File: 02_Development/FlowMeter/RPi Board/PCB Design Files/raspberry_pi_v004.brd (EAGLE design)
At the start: 111.8 x 128.3 mm, 116 parts, among them J5 POWER_JACK, P1 SPL006-007, P2 SPL006-007, P3 SPL006-007, P4 SPL006-007, P5 SPL006-007, Q1 4.3A/20V/54mΩ, Q2 500mA/300V, U6 TCA9548APWR, U7 TCA9548APWR

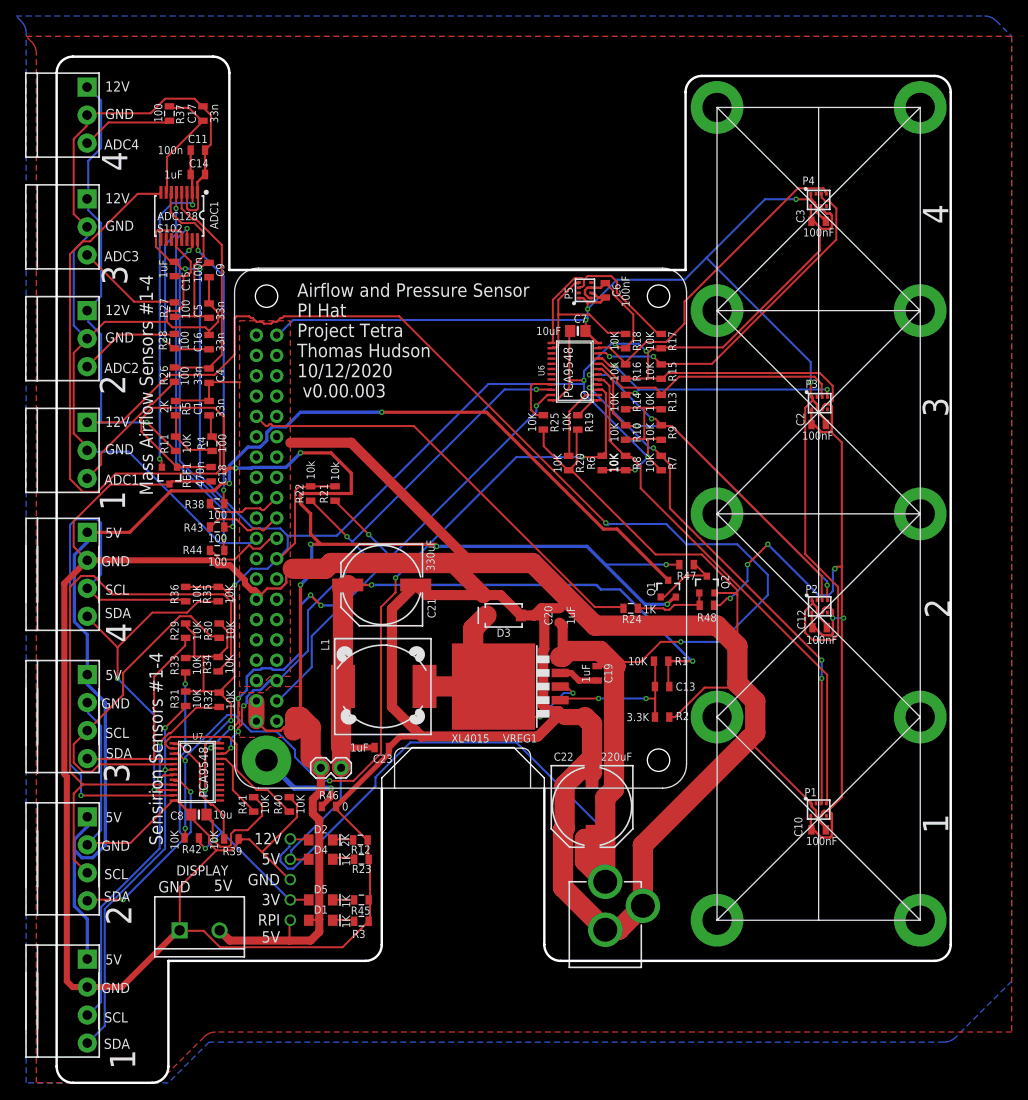
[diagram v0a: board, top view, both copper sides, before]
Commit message: added new 5V regulator
added new 5V regulator as existing regulator was out-of-stock at JLCPCB
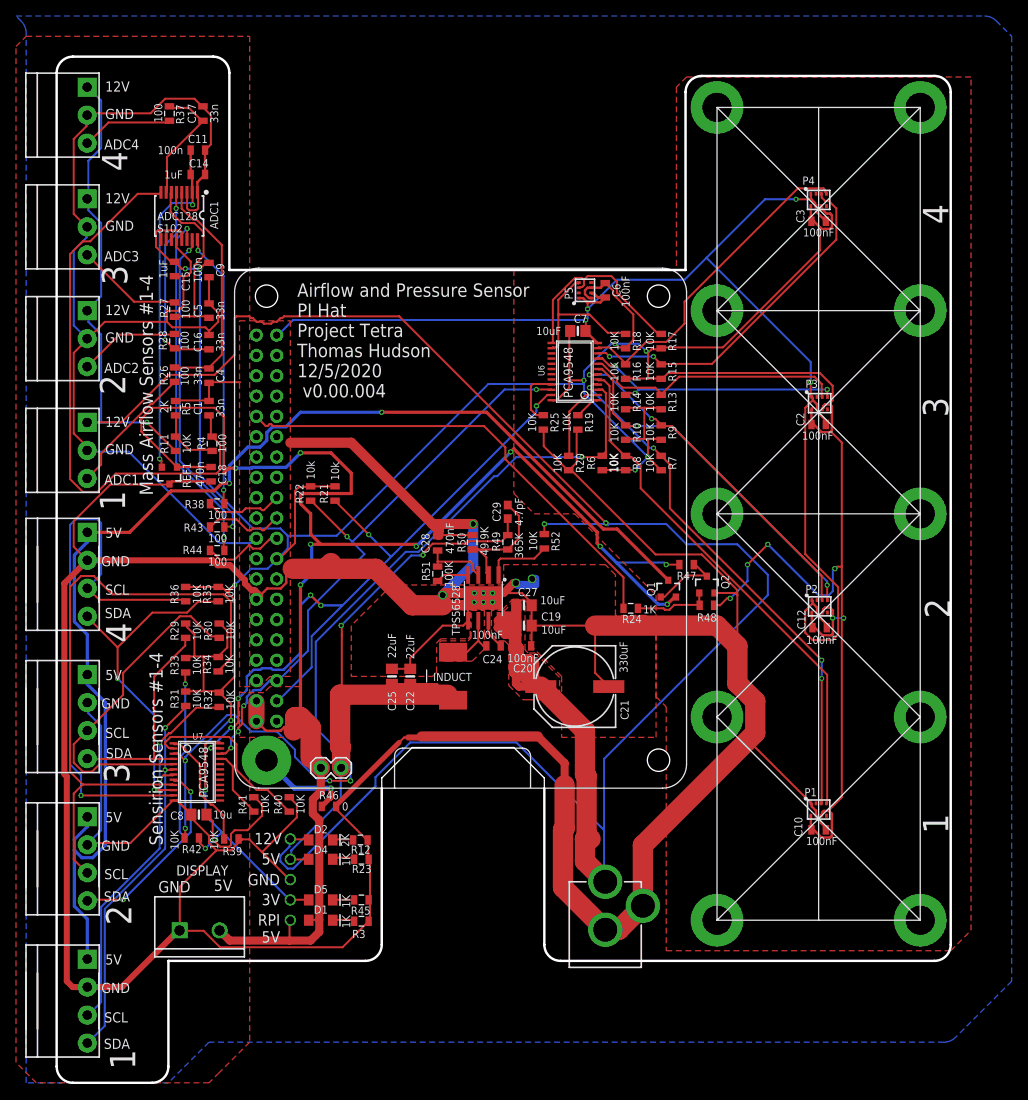
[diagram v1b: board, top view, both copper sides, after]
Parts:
- removed C13: 33n, SparkFun-Capacitors:0805
- removed C23: 1uF, SparkFun-Capacitors:0805
- removed D3: 3A/40V/500mV, SparkFun-DiscreteSemi:SMA-DIODE
- removed L1: INDUCTOR12.5, th_libraries:INDUCTOR_12.5X12.5
- removed R1: 10K, SparkFun-Resistors:0805
- removed R2: 3.3K, SparkFun-Resistors:0805
- removed VREG1: XL4015, th_libraries:TO263-5
- added C24: 100nF, SparkFun-Capacitors:0805
- added C25: 22uF, microbuilder:0805-NO
- added C27: 10uF, microbuilder:0805-NO
- added C28: 470nF, SparkFun-Capacitors:0805
- added C29: 4.7pF, SparkFun-Capacitors:0603
- added INDUCT: INDUCTOR_6.6_7.3, th_libraries:INDUCTOR_6.6_7.3
- added R49: 365K, SparkFun-Passives:0805
- added R50: 49.9K, SparkFun-Passives:0805
- added R51: 100K, SparkFun-Passives:0805
- added R52: 10K, SparkFun-Resistors:0805
- added TPS: TPS56528, th_libraries:SOIC8_POWER
- C19: value 1uF -> 10uF; device SparkFun-Capacitors:0805 -> microbuilder:0805-NO
- C20: value 1uF -> 100nF
- C22: value 220uF -> 22uF; device SparkFun-Capacitors:PANASONIC_G -> microbuilder:0805-NO
- moved C22 27.9 mm to (13.7, -20.3), turned to 90 degrees
- moved C21 27.3 mm to (34.3, -21.6)
- moved C19 10.9 mm to (27.9, -14.0), turned to 0 degrees
- moved C20 5.85 mm to (27.9, -16.5), turned to 0 degrees
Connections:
- new net N$14: C24.1, TPS.7
- new net N$17: R51.1, TPS.4
- new net N$27: R52.2, TPS.1
- net 12V: now also C21.+, C27.1, R52.1, TPS.8; no longer C22.+, VREG1.5
- net 5V: now also C22.1, C25.1, C29.1, INDUCT.2, R49.2; no longer C13.1, C21.+, C23.1, L1.1, R1.1
- net GND: now also C19.2, C22.2, C25.2, C27.2, C28.2, R50.2, TPS.5, TPS.9; no longer C22.-, C23.2, D3.A, R2.2, VREG1.1
- net N$11: now also C29.2, R49.1, R50.1, TPS.2; no longer C13.2, R1.2, R2.1, VREG1.2
- net N$6: now also C24.2, INDUCT.1, TPS.6; no longer D3.C, L1.2, VREG1.3, VREG1.6
- net N$7: now also C28.1, R51.2, TPS.3; no longer C19.2, VREG1.4
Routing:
- net 12V: track 304.9 -> 355.7 mm
- net N$6: track 34.7 -> 7.53 mm, vias 2 -> 0
- net GND: track 900.3 -> 882.2 mm, vias 4 -> 14
- net 5V: track 97.9 -> 85.1 mm
- net PI_5V_POWER: track 202.1 -> 211.8 mm, vias 7 -> 9
- net N$27: track 0.00 -> 8.15 mm
- net N$11: track 21.5 -> 14.9 mm, vias 2 -> 0
- net RESET: track 108.2 -> 112.8 mm
- net N$17: track 0.00 -> 4.12 mm
- net N$14: track 0.00 -> 3.79 mm
- net GPIO12: track 56.0 -> 59.4 mm
- net N$7: track 5.02 -> 8.17 mm
- added copper zone on layer 1, net 12V
- added copper zone on layer 1, net N$6
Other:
- board text added: "Airflow and Pressure Sensor PI Hat Project Tetra Thomas Hudson 12/5/2020 v0.00.004"
- board text removed: "Airflow and Pressure Sensor PI Hat Project Tetra Thomas Hudson 10/12/2020 v0.00.003"

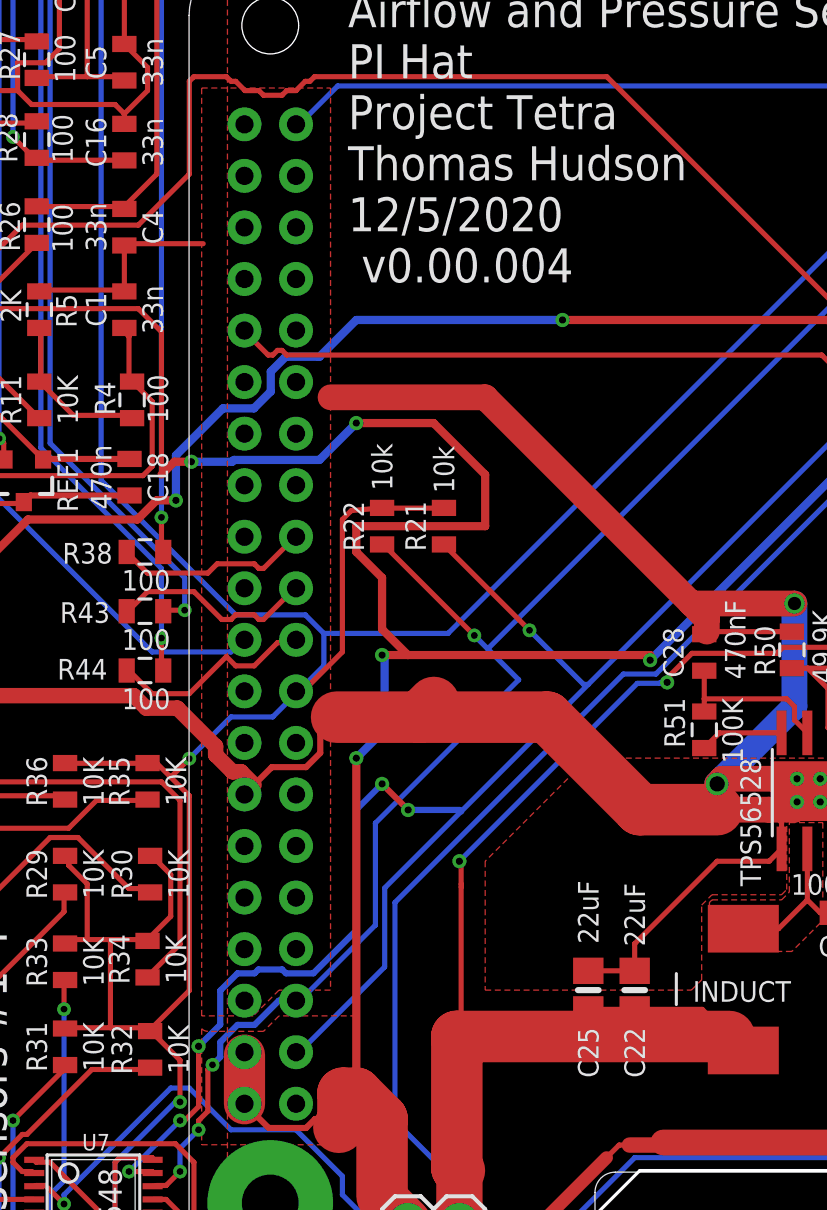
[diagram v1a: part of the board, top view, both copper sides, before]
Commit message: updated capacitor
changed C22 and C25 to 1206 footprint and specified 2mohm low ESR cap
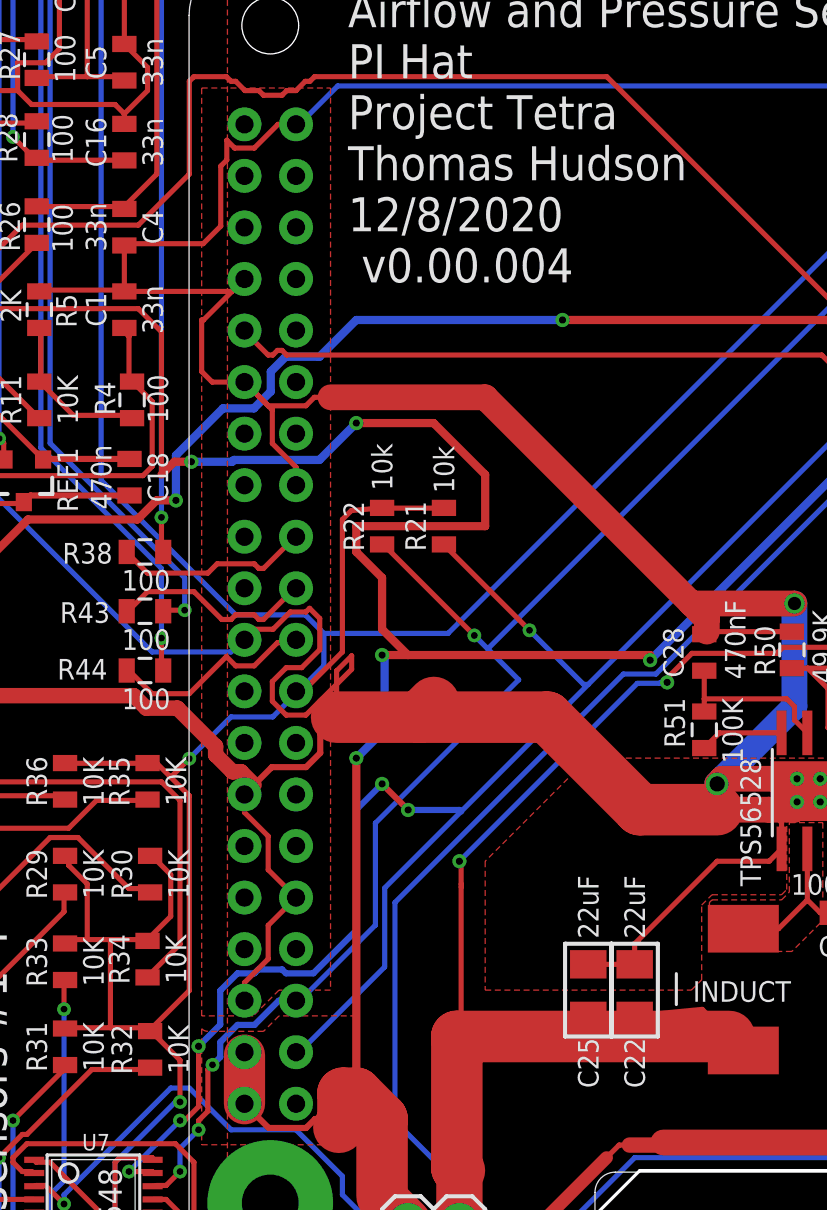
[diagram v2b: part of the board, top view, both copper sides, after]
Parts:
- C22, C25: device microbuilder:0805-NO -> microbuilder:_1206
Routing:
- net GND: track 882.2 -> 948.0 mm
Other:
- board text added: "Airflow and Pressure Sensor PI Hat Project Tetra Thomas Hudson 12/8/2020 v0.00.004"
- board text removed: "Airflow and Pressure Sensor PI Hat Project Tetra Thomas Hudson 12/5/2020 v0.00.004"
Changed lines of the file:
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@@
 Project Tetra
 Thomas Hudson
-12/5/2020
+12/8/2020
  v0.00.004</text>
 <text x="-17.2212" y="-17.2974" size="1.6764" layer="21" ratio="15" rot="R90" align="bottom-right">Sensirion Sensors #1-4</text>
@@
 <attribute name="NAME" x="19" y="-20.895" size="1.016" layer="21" font="vector" ratio="15" align="bottom-center"/>
 </element>
-<element name="C22" library="microbuilder" package="0805-NO" value="22uF" x="13.716" y="-20.32" smashed="yes" rot="R90">
-<attribute name="NAME" x="14.224" y="-24.638" size="1.016" layer="21" ratio="15" rot="R90"/>
-<attribute name="VALUE" x="14.224" y="-18.161" size="1.016" layer="21" ratio="15" rot="R90"/>
-</element>
-<element name="C25" library="microbuilder" package="0805-NO" value="22uF" x="11.43" y="-20.32" smashed="yes" rot="R90">
-<attribute name="NAME" x="11.938" y="-24.638" size="1.016" layer="21" ratio="15" rot="R90"/>
-<attribute name="VALUE" x="11.938" y="-18.034" size="1.016" layer="21" ratio="15" rot="R90"/>
+<element name="C22" library="microbuilder" package="_1206" value="22uF" x="13.716" y="-20.32" smashed="yes" rot="R90">
+<attribute name="NAME" x="14.224" y="-25.146" size="1.016" layer="21" ratio="15" rot="R90"/>
+<attribute name="VALUE" x="14.224" y="-17.78" size="1.016" layer="21" ratio="15" rot="R90"/>
+</element>
+<element name="C25" library="microbuilder" package="_1206" value="22uF" x="11.43" y="-20.32" smashed="yes" rot="R90">
+<attribute name="NAME" x="11.938" y="-25.146" size="1.016" layer="21" ratio="15" rot="R90"/>
+<attribute name="VALUE" x="11.938" y="-17.78" size="1.016" layer="21" ratio="15" rot="R90"/>
 </element>
 </elements>
@@
 <wire x1="35.8902" y1="25.6032" x2="39.5478" y2="29.2608" width="0.254" layer="16"/>
 <wire x1="63.7794" y1="39.3192" x2="63.823546875" y2="39.363346875" width="0.254" layer="1"/>
-<wire x1="-7.5438" y1="16.4592" x2="-11.43" y2="16.4592" width="0.254" layer="1"/>
+<wire x1="-11.43" y1="16.4592" x2="-7.5438" y2="16.4592" width="0.254" layer="1"/>
 <wire x1="-11.43" y1="16.4592" x2="-11.43" y2="16.372" width="0.254" layer="1"/>
 <wire x1="33.6042" y1="5.2578" x2="34.0614" y2="5.2578" width="0.254" layer="1"/>
@@
 <wire x1="-26.647" y1="-59.152" x2="-22.3474" y2="-59.152" width="0.762" layer="1"/>
 <wire x1="-22.3474" y1="-59.152" x2="-15.3162" y2="-52.1208" width="0.762" layer="1"/>
-<wire x1="-1.27" y1="8.89" x2="6.35" y2="8.89" width="1.27" layer="1"/>
+<wire x1="6.35" y1="8.89" x2="-1.27" y2="8.89" width="1.27" layer="1"/>
 <polygon width="2.032" layer="16" isolate="0.000253125">
 <vertex x="-35.56" y="62.23"/>
@@
 <wire x1="33.02" y1="-33.909" x2="33.02" y2="-31.16600625" width="1.016" layer="1"/>
 <wire x1="33.02" y1="-31.16600625" x2="29.68219375" y2="-27.8282" width="1.016" layer="1"/>
-<wire x1="11.43" y1="-19.37" x2="13.716" y2="-19.37" width="0.254" layer="1"/>
+<wire x1="11.43" y1="-19.05" x2="13.716" y2="-19.05" width="0.254" layer="1"/>
 <wire x1="20.955" y1="-13.3604" x2="20.3454" y2="-13.97" width="0.254" layer="1"/>
 <wire x1="20.3454" y1="-13.97" x2="17.78" y2="-13.97" width="0.254" layer="1"/>
 <wire x1="17.78" y1="-13.97" x2="13.716" y2="-18.034" width="0.254" layer="1"/>
-<wire x1="13.716" y1="-18.034" x2="13.716" y2="-19.37" width="0.254" layer="1"/>
+<wire x1="13.716" y1="-18.034" x2="13.716" y2="-19.05" width="0.254" layer="1"/>
 <wire x1="28.89" y1="-11.43" x2="28.89" y2="-13.97" width="0.254" layer="1"/>
 <wire x1="22.86" y1="-10.5156" x2="23.0378" y2="-10.3378" width="0.254" layer="1"/>
@@
 <wire x1="29.337" y1="-8.128" x2="28.956" y2="-8.128" width="1.016" layer="16"/>
 <via x="28.956" y="-8.128" extent="1-16" drill="0.75"/>
+<wire x1="-7.5438" y1="16.4592" x2="-6.6784" y2="17.3246" width="0.254" layer="1"/>
+<wire x1="-6.6784" y1="20.28396875" x2="-6.381184375" y2="20.581184375" width="0.254" layer="1"/>
+<wire x1="-6.381184375" y1="20.581184375" x2="-6.381184375" y2="21.558815625" width="0.254" layer="1"/>
+<wire x1="-6.6784" y1="17.3246" x2="-6.6784" y2="20.28396875" width="0.254" layer="1"/>
+<wire x1="-6.381184375" y1="21.558815625" x2="-5.99396875" y2="21.1716" width="0.254" layer="1"/>
+<wire x1="-5.99396875" y1="21.1716" x2="-5.02603125" y2="21.1716" width="0.254" layer="1"/>
+<wire x1="-3.85763125" y1="22.34" x2="-2.97" y2="22.34" width="0.254" layer="1"/>
+<wire x1="-5.02603125" y1="21.1716" x2="-3.85763125" y2="22.34" width="0.254" layer="1"/>
+<wire x1="-11.43" y1="14.108" x2="-6.122" y2="14.108" width="0.254" layer="1"/>
+<wire x1="-6.122" y1="14.108" x2="-5.51" y2="14.72" width="0.254" layer="1"/>
+<wire x1="-5.51" y1="14.72" x2="-7.53" y2="12.7" width="0.254" layer="1"/>
+<wire x1="-7.53" y1="12.7" x2="-7.62" y2="12.7" width="0.254" layer="1"/>
+<wire x1="-7.62" y1="12.7" x2="-7.62" y2="10.16" width="0.254" layer="1"/>
+<wire x1="-7.62" y1="10.16" x2="-7.1" y2="9.64" width="0.254" layer="1"/>
+<wire x1="-7.1" y1="9.64" x2="-5.51" y2="9.64" width="0.254" layer="1"/>
+<wire x1="-1.27" y1="8.89" x2="-2.06763125" y2="8.89" width="0.254" layer="1"/>
+<wire x1="-2.06763125" y1="8.89" x2="-2.48603125" y2="8.4716" width="0.254" layer="1"/>
+<wire x1="-2.48603125" y1="8.4716" x2="-4.3416" y2="8.4716" width="0.254" layer="1"/>
+<wire x1="-4.3416" y1="8.4716" x2="-5.51" y2="9.64" width="0.254" layer="1"/>
+<wire x1="-5.51" y1="9.64" x2="-4.1384" y2="8.2684" width="0.254" layer="1"/>
+<wire x1="-2.97" y1="5.44763125" x2="-2.97" y2="4.56" width="0.254" layer="1"/>
+<wire x1="-4.1384" y1="8.2684" x2="-4.1384" y2="6.61603125" width="0.254" layer="1"/>
+<wire x1="-4.1384" y1="6.61603125" x2="-2.97" y2="5.44763125" width="0.254" layer="1"/>
+<wire x1="-5.51" y1="-20.84" x2="-5.51" y2="-19.95236875" width="0.254" layer="1"/>
+<wire x1="-4.3416" y1="-17.1316" x2="-2.97" y2="-15.76" width="0.254" layer="1"/>
+<wire x1="-5.51" y1="-19.95236875" x2="-4.3416" y2="-18.78396875" width="0.254" layer="1"/>
+<wire x1="-4.3416" y1="-18.78396875" x2="-4.3416" y2="-17.1316" width="0.254" layer="1"/>
+<wire x1="-2.97" y1="-15.76" x2="-4.3416" y2="-14.3884" width="0.254" layer="1"/>
+<wire x1="-5.51" y1="-11.56763125" x2="-5.51" y2="-10.68" width="0.254" layer="1"/>
+<wire x1="-4.3416" y1="-14.3884" x2="-4.3416" y2="-12.73603125" width="0.254" layer="1"/>
+<wire x1="-4.3416" y1="-12.73603125" x2="-5.51" y2="-11.56763125" width="0.254" layer="1"/>
+<wire x1="-5.51" y1="-3.06" x2="-4.99" y2="-2.54" width="0.254" layer="1"/>
+<wire x1="-4.99" y1="-2.54" x2="-4.10236875" y2="-2.54" width="0.254" layer="1"/>
+<wire x1="-3.25076875" y1="-1.6884" x2="-2.48603125" y2="-1.6884" width="0.254" layer="1"/>
+<wire x1="-2.48603125" y1="-1.6884" x2="-2.303815625" y2="-1.506184375" width="0.254" layer="1"/>
+<wire x1="-3.45396875" y1="-4.4316" x2="-4.1384" y2="-5.11603125" width="0.254" layer="1"/>
+<wire x1="-4.1384" y1="-5.11603125" x2="-4.1384" y2="-6.08396875" width="0.254" layer="1"/>
+<wire x1="-4.1384" y1="-6.08396875" x2="-3.45396875" y2="-6.7684" width="0.254" layer="1"/>
+<wire x1="-3.45396875" y1="-6.7684" x2="-2.48603125" y2="-6.7684" width="0.254" layer="1"/>
+<wire x1="-2.303815625" y1="-1.506184375" x2="-1.8016" y2="-2.0084" width="0.254" layer="1"/>
+<wire x1="-1.8016" y1="-2.0084" x2="-1.8016" y2="-3.54396875" width="0.254" layer="1"/>
+<wire x1="-1.8016" y1="-3.54396875" x2="-2.68923125" y2="-4.4316" width="0.254" layer="1"/>
+<wire x1="-2.68923125" y1="-4.4316" x2="-3.45396875" y2="-4.4316" width="0.254" layer="1"/>
+<wire x1="-2.48603125" y1="-6.7684" x2="-0.2286" y2="-4.51096875" width="0.254" layer="1"/>
+<wire x1="-0.2286" y1="-4.51096875" x2="-0.2286" y2="-3.84698125" width="0.254" layer="1"/>
+<wire x1="-0.97118125" y1="-4.5895625" x2="-0.97118125" y2="-6.87" width="0.254" layer="1"/>
+<wire x1="-0.2286" y1="-3.84698125" x2="-0.97118125" y2="-4.5895625" width="0.254" layer="1"/>
+<wire x1="-4.10236875" y1="-2.54" x2="-3.25076875" y2="-1.6884" width="0.254" layer="1"/>
 </signal>
 <signal name="SCL">
@@
 <wire x1="19.07" y1="-23.295" x2="18.381" y2="-22.606" width="0.254" layer="1"/>
 <wire x1="19.07" y1="-23.295" x2="17.045" y2="-21.27" width="0.254" layer="1"/>
-<wire x1="17.045" y1="-21.27" x2="13.716" y2="-21.27" width="0.254" layer="1"/>
-<wire x1="13.716" y1="-21.27" x2="11.43" y2="-21.27" width="0.254" layer="1"/>
+<wire x1="17.045" y1="-21.27" x2="13.716" y2="-21.59" width="0.254" layer="1"/>
+<wire x1="13.716" y1="-21.59" x2="11.43" y2="-21.59" width="0.254" layer="1"/>
 <wire x1="16.535225" y1="-3.7258" x2="15.24" y2="-5.021025" width="0.254" layer="1"/>
 <wire x1="15.24" y1="-5.021025" x2="15.24" y2="-5.08" width="0.254" layer="1"/>
